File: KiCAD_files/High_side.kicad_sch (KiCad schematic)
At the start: 27 parts, among them U204 MCP6486UT-E/LT, U601 AMC1311DWV, U602 +-20A Hall

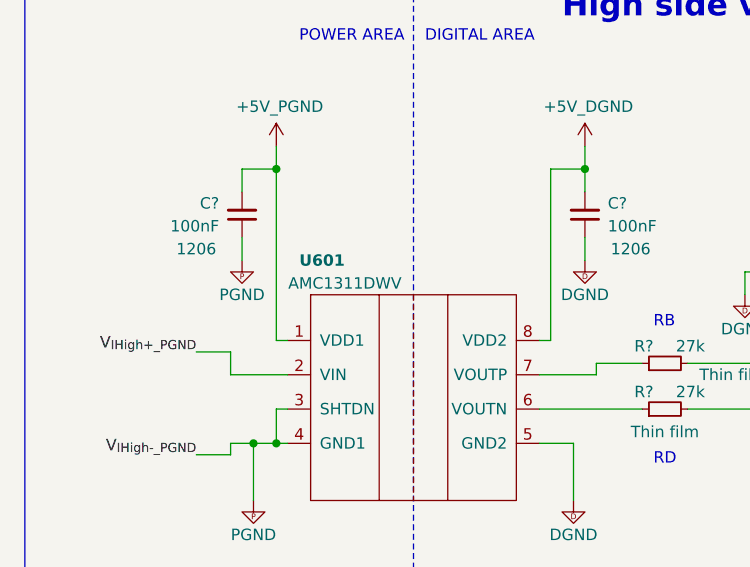
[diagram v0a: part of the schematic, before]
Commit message: modified manf so BOM matches the order
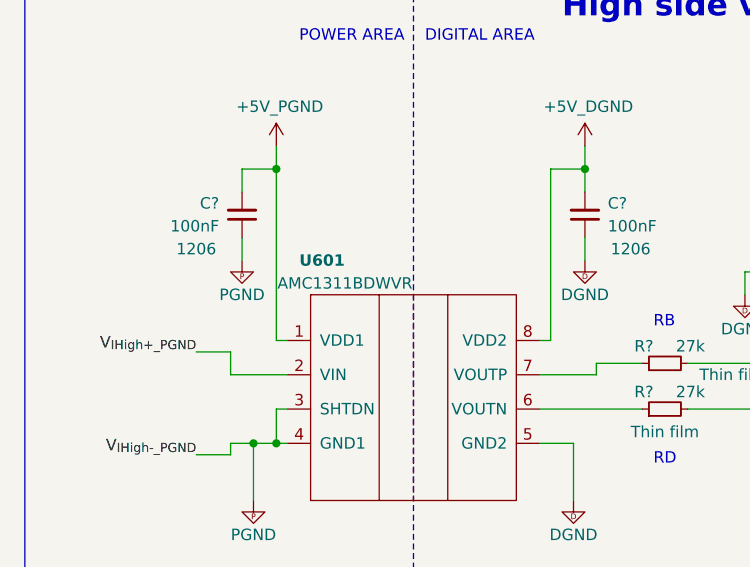
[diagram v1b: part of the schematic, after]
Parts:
- R217: manf# RT0805DRE075K9L -> RR1220P-5901-D-M
- U601: value AMC1311DWV -> AMC1311BDWVR; manf# AMC1311DWV -> AMC1311BDWVR
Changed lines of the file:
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@@
       (effects (font (size 1.27 1.27)) hide)
     )
-    (property "Datasheet" "${KIPRJMOD}\\datasheet\\PYu_RT_1_to_0_01_RoHS_L_12-3003070.pdf" (at 240.03 208.28 0)
-      (effects (font (size 1.27 1.27)) hide)
-    )
-    (property "manf#" "RT0805DRE075K9L" (at 240.03 208.28 0)
+    (property "Datasheet" "${KIPRJMOD}\\datasheet\\susumu_RR_Data_Sheet-1206438.pdf" (at 240.03 208.28 0)
+      (effects (font (size 1.27 1.27)) hide)
+    )
+    (property "manf#" "RR1220P-5901-D-M" (at 240.03 208.28 0)
       (effects (font (size 1.27 1.27)) hide)
     )
@@
       (effects (font (size 1.27 1.27)) hide)
     )
-    (property "Datasheet" "${KIPRJMOD}\\datasheet\\PYu_RT_1_to_0_01_RoHS_L_12-3003070.pdf" (at 217.17 186.69 0)
-      (effects (font (size 1.27 1.27)) hide)
-    )
-    (property "manf#" "RT0805DRE075K9L" (at 217.17 186.69 0)
+    (property "Datasheet" "${KIPRJMOD}\\datasheet\\susumu_RR_Data_Sheet-1206438.pdf" (at 217.17 186.69 0)
+      (effects (font (size 1.27 1.27)) hide)
+    )
+    (property "manf#" "RR1220P-5901-D-M" (at 217.17 186.69 0)
       (effects (font (size 1.27 1.27)) hide)
     )
@@
       (effects (font (size 1.27 1.27) bold))
     )
-    (property "Value" "AMC1311DWV" (at 53.34 182.88 0)
+    (property "Value" "AMC1311BDWVR" (at 53.34 182.88 0)
       (effects (font (size 1.27 1.27)))
     )
@@
       (effects (font (size 1.27 1.27)) hide)
     )
-    (property "manf#" "AMC1311DWV" (at 52.07 208.28 0)
-      (effects (font (size 1.27 1.27)) hide)
-    )
+    (property "manf#" "AMC1311BDWVR" (at 52.07 208.28 0)
+      (effects (font (size 1.27 1.27)) hide)
+    )

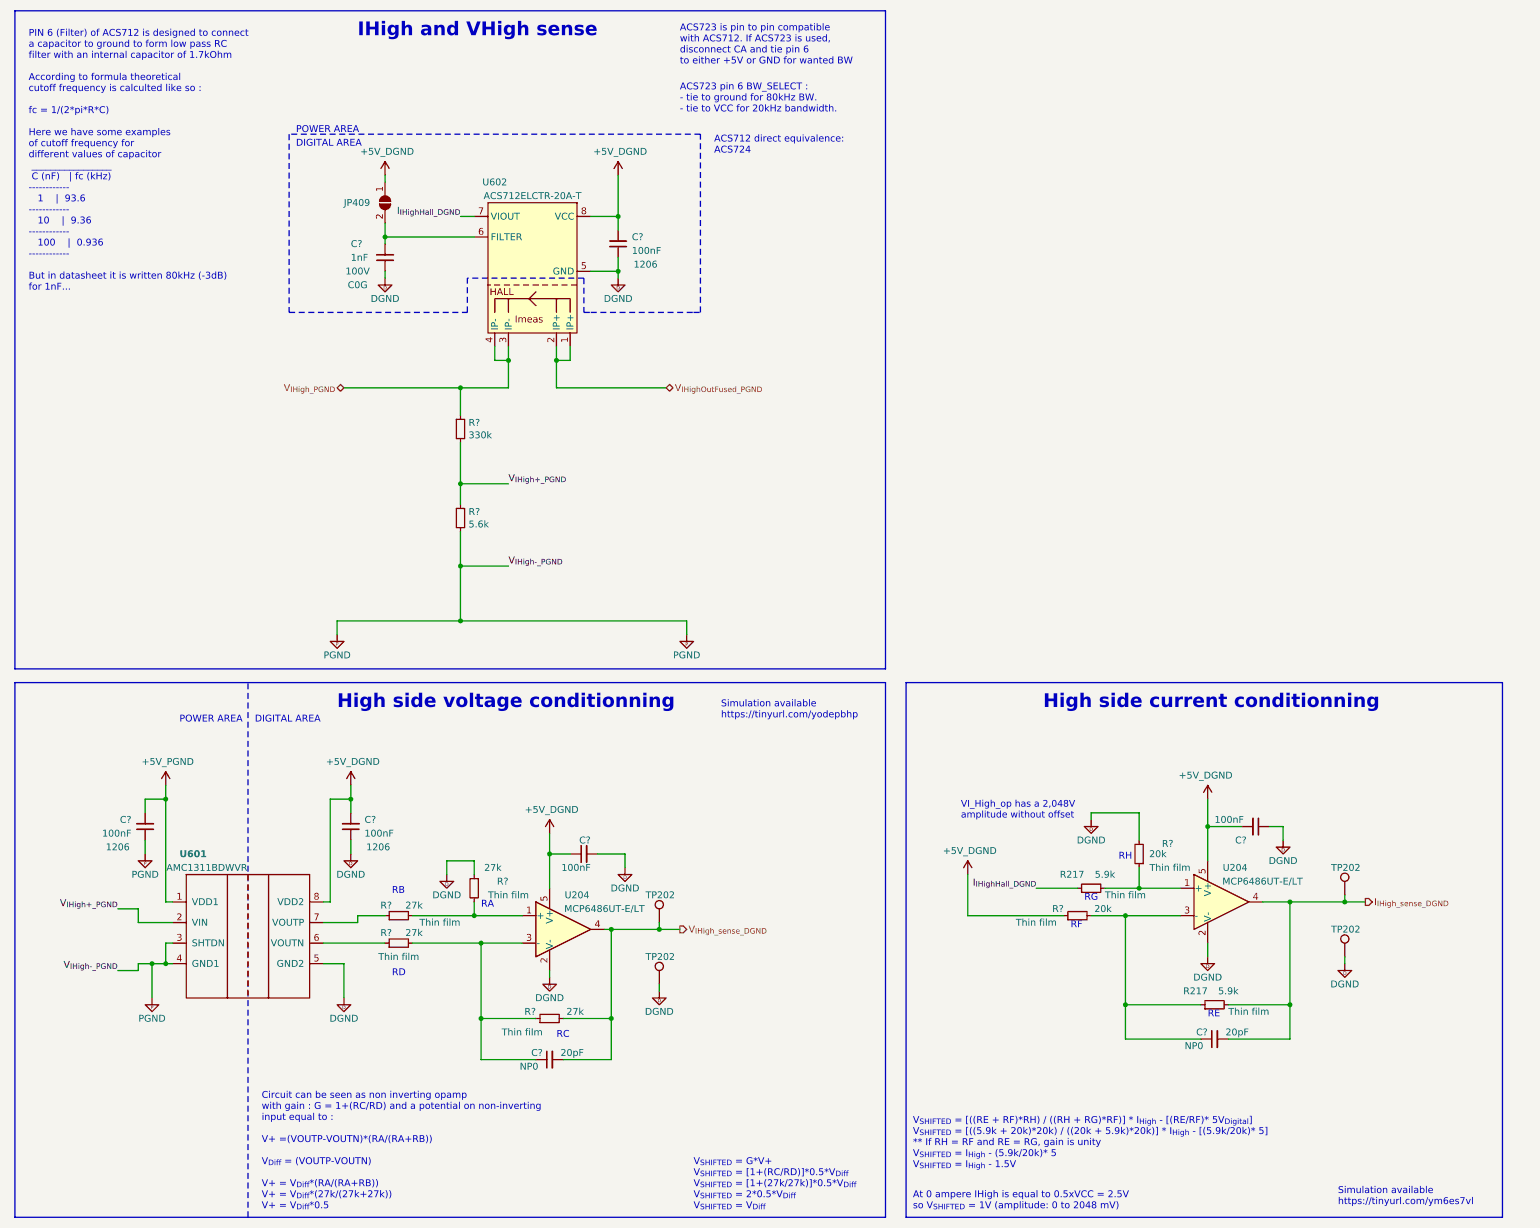
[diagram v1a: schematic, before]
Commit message: Added missing In.Cu1 DGND where missing Supressed duplicated copper zones Checked inner copper layers Added missing thermal brakes Spaced components in feeder Optimized few component placements Corrected schematic language mistakes
Signed-off-by: Jean Alinei <jean.alinei@laas.fr>
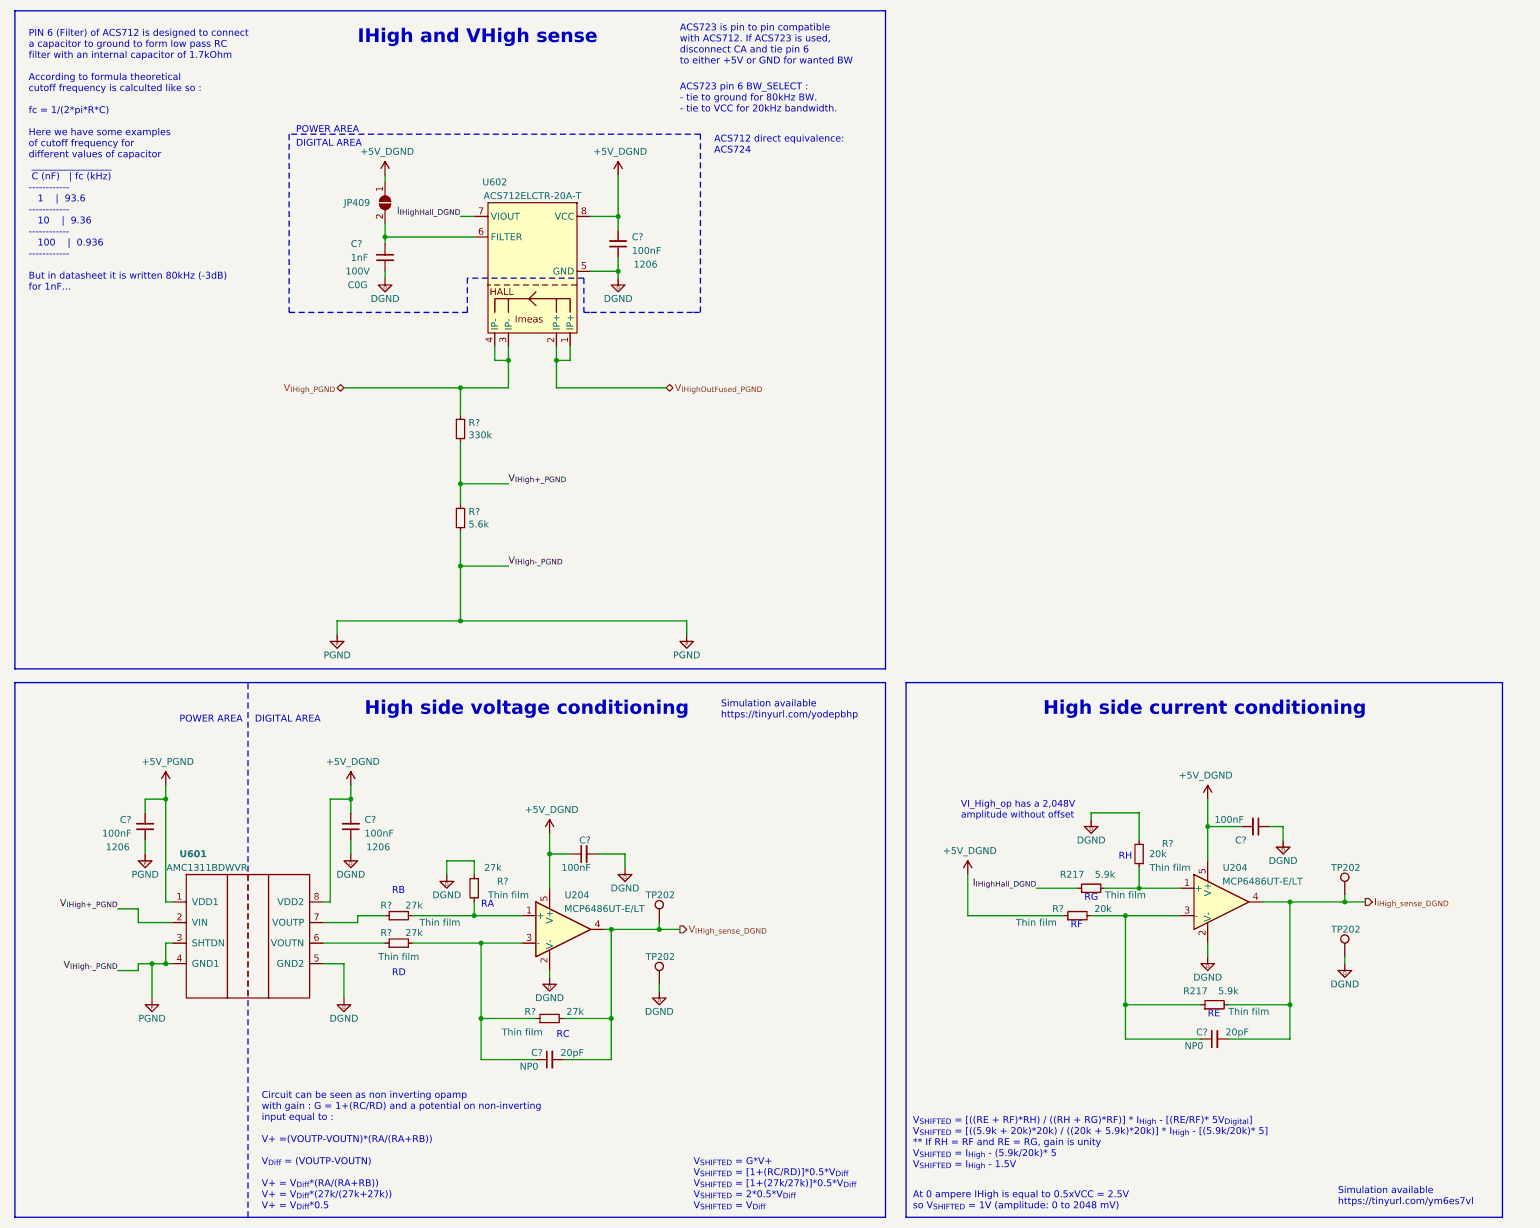
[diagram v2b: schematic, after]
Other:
- note added: "High side current conditioning"
- note added: "High side voltage conditioning"
- note removed: "High side current conditionning"
- note removed: "High side voltage conditionning"
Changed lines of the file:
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@@
     (effects (font (size 1.27 1.27)) (justify left bottom))
   )
-  (text "IHigh and VHigh sense\n" (at 125.73 29.21 0)
+  (text "IHigh and VHigh sense\n" (at 125.73 30.48 0)
     (effects (font (face "Arial") (size 2.54 2.54) (thickness 0.4978) bold) (justify right bottom))
   )
@@
     (effects (font (size 1.27 1.27)) (justify left bottom))
   )
-  (text "High side voltage conditionning" (at 77.47 153.67 0)
+  (text "High side voltage conditioning" (at 82.55 154.94 0)
     (effects (font (size 2.54 2.54) (thickness 0.5) bold) (justify left bottom))
   )
@@
     (effects (font (size 1.27 1.27)) (justify left bottom))
   )
-  (text "High side current conditionning" (at 208.28 153.67 0)
+  (text "High side current conditioning" (at 208.28 154.94 0)
     (effects (font (size 2.54 2.54) (thickness 0.5) bold) (justify left bottom))
   )

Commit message: DNP field set to empty for C601, 603, 604 ,606, 608, R607, 609
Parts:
- C? (x5), R? (x2): DNP x -> (none)
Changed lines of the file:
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@@
       (effects (font (size 1.27 1.27)) hide)
     )
-    (property "DNP" "x" (at 80.01 175.26 0)
+    (property "DNP" "" (at 80.01 175.26 0)
       (effects (font (size 1.27 1.27)) hide)
     )
@@
       (effects (font (size 1.27 1.27)) hide)
     )
-    (property "DNP" "x" (at 226.06 180.34 0)
+    (property "DNP" "" (at 226.06 180.34 0)
       (effects (font (size 1.27 1.27)) hide)
     )
@@
       (effects (font (size 1.27 1.27)) hide)
     )
-    (property "DNP" "x" (at 247.65 175.26 0)
+    (property "DNP" "" (at 247.65 175.26 0)
       (effects (font (size 1.27 1.27)) hide)
     )
@@
       (effects (font (size 1.27 1.27)) hide)
     )
-    (property "DNP" "x" (at 129.54 67.31 0)
+    (property "DNP" "" (at 129.54 67.31 0)
       (effects (font (size 1.27 1.27)) hide)
     )
@@
       (effects (font (size 1.27 1.27)) hide)
     )
-    (property "DNP" "x" (at 214.63 191.77 0)
+    (property "DNP" "" (at 214.63 191.77 0)
       (effects (font (size 1.27 1.27)) hide)
     )
@@
       (effects (font (size 1.27 1.27)) hide)
     )
-    (property "DNP" "x" (at 41.91 175.26 0)
+    (property "DNP" "" (at 41.91 175.26 0)
       (effects (font (size 1.27 1.27)) hide)
     )
@@
       (effects (font (size 1.27 1.27)) hide)
     )
-    (property "DNP" "x" (at 123.19 180.34 0)
-      (effects (font (size 1.27 1.27)) hide)
-    )
+    (property "DNP" "" (at 123.19 180.34 0)
+      (effects (font (size 1.27 1.27)) hide)
+    )

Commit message: Added BOOT0 pull down - Checked PMOS rerouting Suppress thermal reliefs on LEG1 high side. Suppress copper finger below inductors. Moved resistors close to OAmp to make silkscreen better
Signed-off-by: Jean Alinei <jean.alinei@laas.fr>
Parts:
- gave numbers to parts that had none: 8
- renumbered JP409 to JP601, R217 to R608, R217 to R610, TP202 to TP601, TP202 to TP602, TP202 to TP603, TP202 to TP604, U204 to U603, U204 to U604

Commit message: TWIST V1.4.1
Signed-off-by: Jean Alinei <jean.alinei@owntech.org>
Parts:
- C605, C607: Reserved1 (none) -> 269e10abb8e08bedf6fe59138f738c816916bbb2d9
- C? (x5): Reserved1 (none) -> bd09595a5e7ca1766022111bddfe0f5a6e4908a36b93
- C?: Reserved1 (none) -> 36d65648c9f9763ce523fbb2fa348ea74e1ffbece389
- R601: Reserved1 (none) -> de80908cc82a0210b1e2e612ccfd739eec83c979ef0a
- R602: Reserved1 (none) -> 67db2c24762cea30e11f13dd39d2663e9787eb3eef
- R603, R604, R605, R606: Reserved1 (none) -> c13f1324e4589c70b04383b2cc819b3b2aa93ba236a3
- R608, R610: Reserved1 (none) -> ed585694ae6eb04ca3ae177c490503548b02c4354fb4
- R? (x2): Reserved1 (none) -> 4e62068438486240cd804b758ba9b5cf82f9e4c51a
- U601: Reserved1 (none) -> 9146999d21d909e45759155956b4a63f323089ea7408d5
- U602: Reserved1 (none) -> f828c72a27a18effc44b64d9a0faef86c299c4bb3f04
- U603, U604: value MCP6486UT-E/LT -> MCP6486UT-E/LT; Reserved1 (none) -> a2d385477ecd4c4b3c668075cae345766bdddc95fe7cb2e1

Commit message: Initial commit TWIST V1.4.2
Signed-off-by: Jean Alinei <jean.alinei@owntech.org>
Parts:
- gave numbers to parts that had none: 8
